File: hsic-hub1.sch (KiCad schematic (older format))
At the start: 32 parts

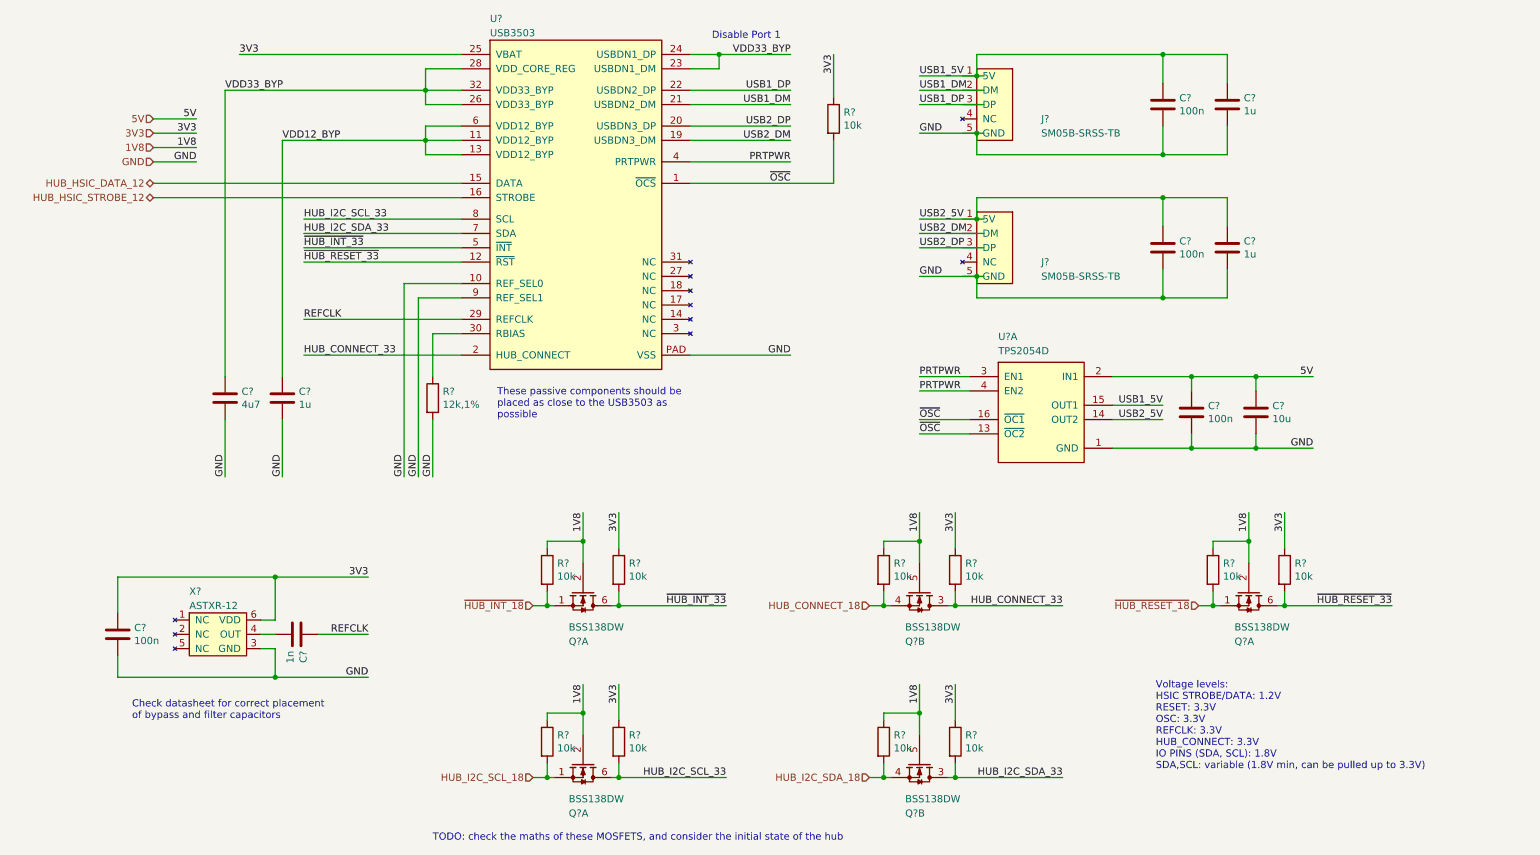
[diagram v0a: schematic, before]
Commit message: Add I2C level shifting and the two HSIC hubs.
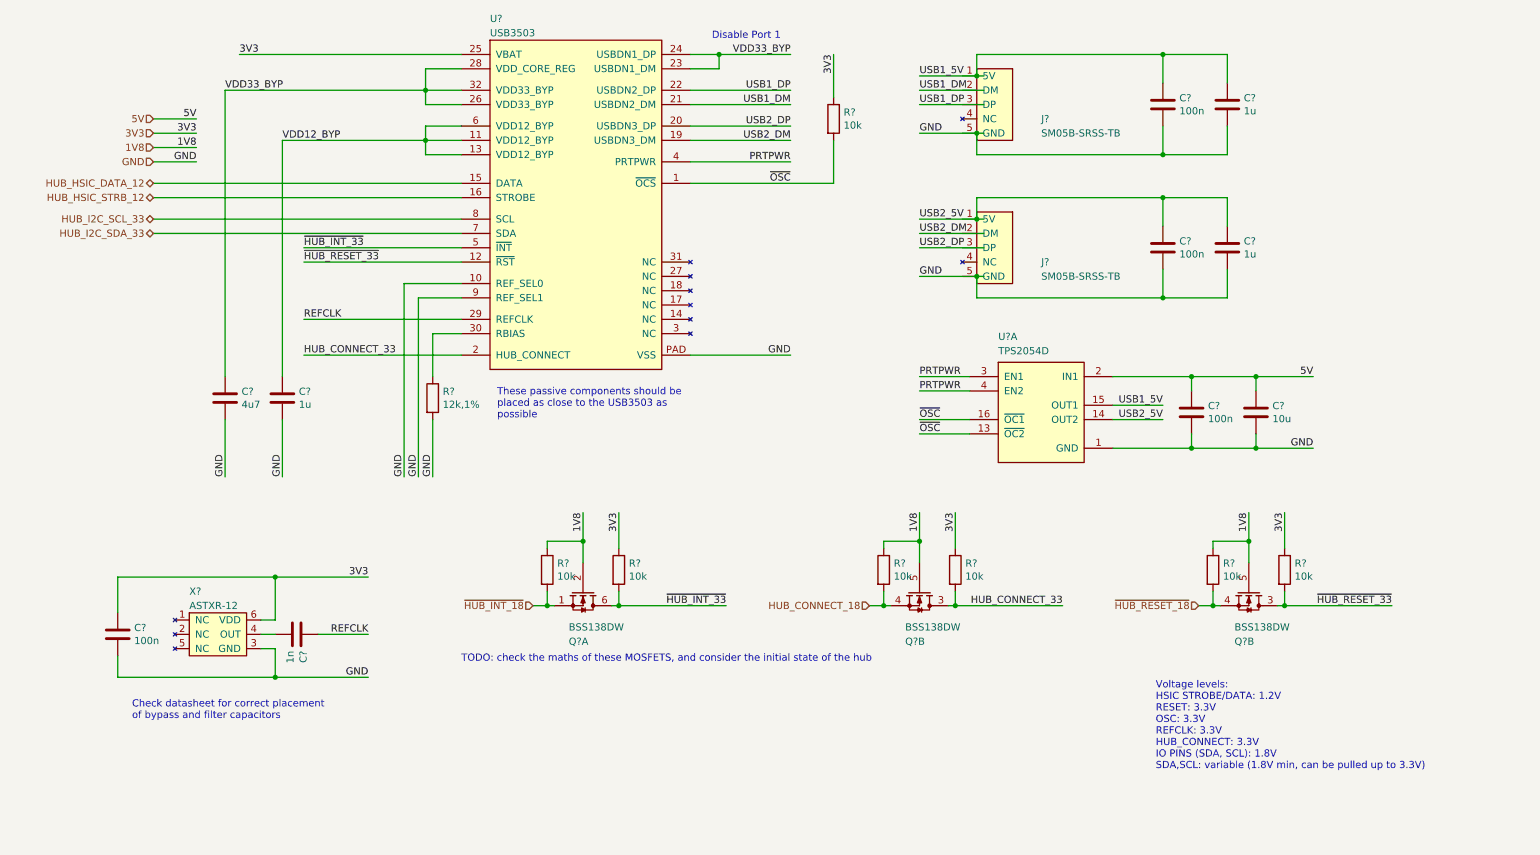
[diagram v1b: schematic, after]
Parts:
- removed Q? (x3): BSS138DW, symbol Drone:BSS138DW
- removed R? (x4): 10k, symbol Device:R
- added Q?: BSS138DW, symbol Drone:BSS138DW
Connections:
- net labels added: HUB_HSIC_STRB_12
- net labels removed: HUB_HSIC_STROBE_12, HUB_I2C_SCL_18, HUB_I2C_SDA_18
- wire segments 164 -> 142
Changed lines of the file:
@@
 $Descr A4 11693 8268
 encoding utf-8
-Sheet 2 3
+Sheet 4 4
 Title ""
 Date ""
@@
 	1400 1850 3550 1850
 Text HLabel 1400 1950 0    50   BiDi ~ 0
-HUB_HSIC_STROBE_12
+HUB_HSIC_STRB_12
 Text HLabel 1400 1850 0    50   BiDi ~ 0
 HUB_HSIC_DATA_12
@@
 AR Path="/5E2B9068/5E2F42C0" Ref="U?"  Part="1"
 AR Path="/5E2EDC4D/5E2F42C0" Ref="U?"  Part="1"
+AR Path="/5E349830/5E2F42C0" Ref="U?"  Part="1"
 F 0 "U?" H 3750 1000 50  0000 L CNN
 F 1 "USB3503" H 3750 900 50  0000 L CNN
@@
 	1700 1500 1400 1500
 Wire Wire Line
-	2450 2200 3550 2200
-Wire Wire Line
-	2450 2100 3550 2100
+	1400 2200 3550 2200
+Wire Wire Line
+	1400 2100 3550 2100
 Wire Wire Line
 	2450 2400 3550 2400
@@
 	1    0    0    -1
 $EndComp
-Text Label 2450 2100 0    50   ~ 0
-HUB_I2C_SCL_33
-Text Label 2450 2200 0    50   ~ 0
-HUB_I2C_SDA_33
 Text Label 2450 2300 0    50   ~ 0
 ~HUB_INT_33
@@
 HUB_CONNECT_33
 $Comp
-L Drone:BSS138DW Q?
-U 1 1 5E5F6987
-P 9050 4800
-F 0 "Q?" V 9300 4700 50  0000 L CNN
-F 1 "BSS138DW" V 9200 4700 50  0000 L CNN
-F 2 "" H 9150 4725 50  0001 L CIN
-F 3 "https://www.diodes.com/assets/Datasheets/ds30203.pdf" H 8950 4800 50  0001 L CNN
-	1    9050 4800
-	0    1    1    0
-$EndComp
-$Comp
 L Device:R R?
 U 1 1 5E5F698D
@@
 Text HLabel 8700 4800 0    50   Input ~ 0
 ~HUB_RESET_18
-$Comp
-L Drone:BSS138DW Q?
-U 2 1 5E636D9D
-P 6750 6000
-F 0 "Q?" V 7000 5900 50  0000 L CNN
-F 1 "BSS138DW" V 6900 5900 50  0000 L CNN
-F 2 "" H 6850 5925 50  0001 L CIN
-F 3 "https://www.diodes.com/assets/Datasheets/ds30203.pdf" H 6650 6000 50  0001 L CNN
-	2    6750 6000
-	0    1    1    0
-$EndComp
-$Comp
-L Device:R R?
-U 1 1 5E636DA3
-P 7000 5750
-F 0 "R?" H 7070 5796 50  0000 L CNN
-F 1 "10k" H 7070 5705 50  0000 L CNN
-F 2 "" V 6930 5750 50  0001 C CNN
-F 3 "~" H 7000 5750 50  0001 C CNN
-	1    7000 5750
-	1    0    0    -1
-$EndComp
-Text Label 7000 5350 3    50   ~ 0
-3V3
-Wire Wire Line
-	7000 5350 7000 5600
-Wire Wire Line
-	7000 5900 7000 6000
-Wire Wire Line
-	7000 6000 6950 6000
-Text Label 6750 5350 3    50   ~ 0
-1V8
-Wire Wire Line
-	6750 5350 6750 5550
-$Comp
-L Device:R R?
-U 1 1 5E636DAF
-P 6500 5750
-F 0 "R?" H 6570 5796 50  0000 L CNN
-F 1 "10k" H 6570 5705 50  0000 L CNN
-F 2 "" V 6430 5750 50  0001 C CNN
-F 3 "~" H 6500 5750 50  0001 C CNN
-	1    6500 5750
-	1    0    0    -1
-$EndComp
-Wire Wire Line
-	6500 5600 6500 5550
-Wire Wire Line
-	6500 5550 6750 5550
-Connection ~ 6750 5550
-Wire Wire Line
-	6750 5550 6750 5700
-Wire Wire Line
-	6550 6000 6500 6000
-Wire Wire Line
-	6500 6000 6500 5900
-Wire Wire Line
-	6500 6000 6400 6000
-Connection ~ 6500 6000
-Text HLabel 6400 6000 0    50   Input ~ 0
-HUB_I2C_SDA_18
-$Comp
-L Drone:BSS138DW Q?
-U 1 1 5E636DBE
-P 4400 6000
-F 0 "Q?" V 4650 5900 50  0000 L CNN
-F 1 "BSS138DW" V 4550 5900 50  0000 L CNN
-F 2 "" H 4500 5925 50  0001 L CIN
-F 3 "https://www.diodes.com/assets/Datasheets/ds30203.pdf" H 4300 6000 50  0001 L CNN
-	1    4400 6000
-	0    1    1    0
-$EndComp
-$Comp
-L Device:R R?
-U 1 1 5E636DC4
-P 4650 5750
-F 0 "R?" H 4720 5796 50  0000 L CNN
-F 1 "10k" H 4720 5705 50  0000 L CNN
-F 2 "" V 4580 5750 50  0001 C CNN
-F 3 "~" H 4650 5750 50  0001 C CNN
-	1    4650 5750
-	1    0    0    -1
-$EndComp
-Text Label 4650 5350 3    50   ~ 0
-3V3
-Wire Wire Line
-	4650 5350 4650 5600
-Wire Wire Line
-	4650 5900 4650 6000
-Wire Wire Line
-	4650 6000 4600 6000
-Text Label 4400 5350 3    50   ~ 0
-1V8
-Wire Wire Line
-	4400 5350 4400 5550
-$Comp
-L Device:R R?
-U 1 1 5E636DD0
-P 4150 5750
-F 0 "R?" H 4220 5796 50  0000 L CNN
-F 1 "10k" H 4220 5705 50  0000 L CNN
-F 2 "" V 4080 5750 50  0001 C CNN
-F 3 "~" H 4150 5750 50  0001 C CNN
-	1    4150 5750
-	1    0    0    -1
-$EndComp
-Wire Wire Line
-	4150 5600 4150 5550
-Wire Wire Line
-	4150 5550 4400 5550
-Connection ~ 4400 5550
-Wire Wire Line
-	4400 5550 4400 5700
-Wire Wire Line
-	4200 6000 4150 6000
-Wire Wire Line
-	4150 6000 4150 5900
-Wire Wire Line
-	4150 6000 4050 6000
-Connection ~ 4150 6000
-Wire Wire Line
-	4650 6000 5400 6000
-Connection ~ 4650 6000
-Text HLabel 4050 6000 0    50   Input ~ 0
-HUB_I2C_SCL_18
-Connection ~ 7000 6000
-Wire Wire Line
-	7000 6000 7750 6000
-Text Label 5400 6000 2    50   ~ 0
-HUB_I2C_SCL_33
-Text Label 7750 6000 2    50   ~ 0
-HUB_I2C_SDA_33
 Text Notes 8400 5950 0    50   ~ 0
 Voltage levels:\nHSIC STROBE/DATA: 1.2V\nRESET: 3.3V\nOSC: 3.3V\nREFCLK: 3.3V\nHUB_CONNECT: 3.3V\nIO PINS (SDA, SCL): 1.8V\nSDA,SCL: variable (1.8V min, can be pulled up to 3.3V)
-Text Notes 3350 6450 0    50   ~ 0
+Text Notes 3550 5200 0    50   ~ 0
 TODO: check the maths of these MOSFETS, and consider the initial state of the hub
+Text HLabel 1400 2100 0    50   BiDi ~ 0
+HUB_I2C_SCL_33
+Text HLabel 1400 2200 0    50   BiDi ~ 0
+HUB_I2C_SDA_33
+$Comp
+L Drone:BSS138DW Q?
+U 2 1 5E532DF9
+P 9050 4800
+AR Path="/5E2EDC4D/5E532DF9" Ref="Q?"  Part="2"
+AR Path="/5E349830/5E532DF9" Ref="Q?"  Part="2"
+F 0 "Q?" V 9300 4700 50  0000 L CNN
+F 1 "BSS138DW" V 9200 4700 50  0000 L CNN
+F 2 "" H 9150 4725 50  0001 L CIN
+F 3 "https://www.diodes.com/assets/Datasheets/ds30203.pdf" H 8950 4800 50  0001 L CNN
+	2    9050 4800
+	0    1    1    0
+$EndComp
 $EndSCHEMATC

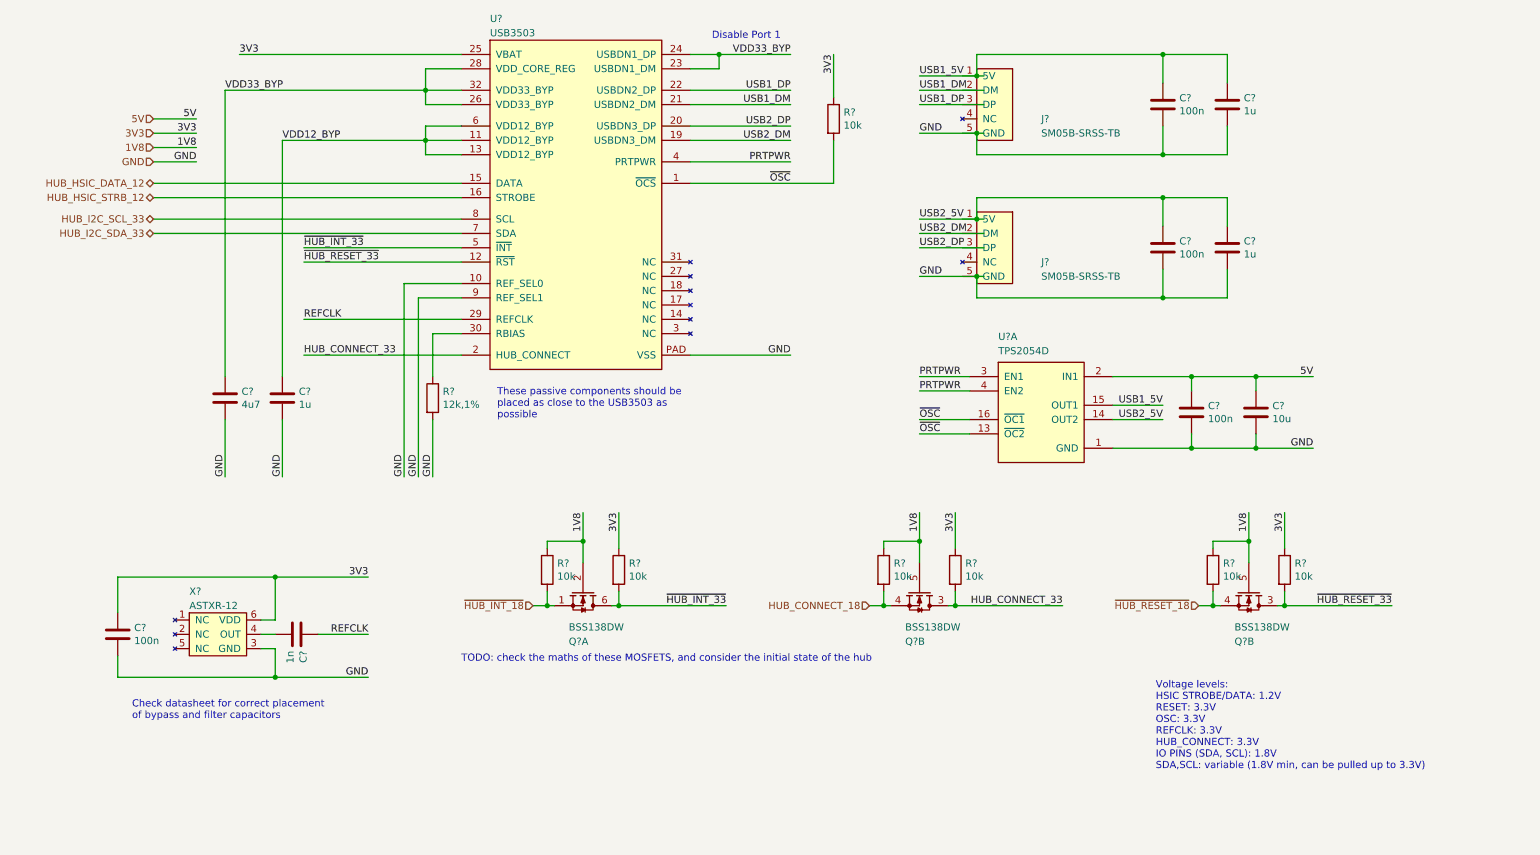
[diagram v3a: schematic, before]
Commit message: Added GPIO expander for hub signals.
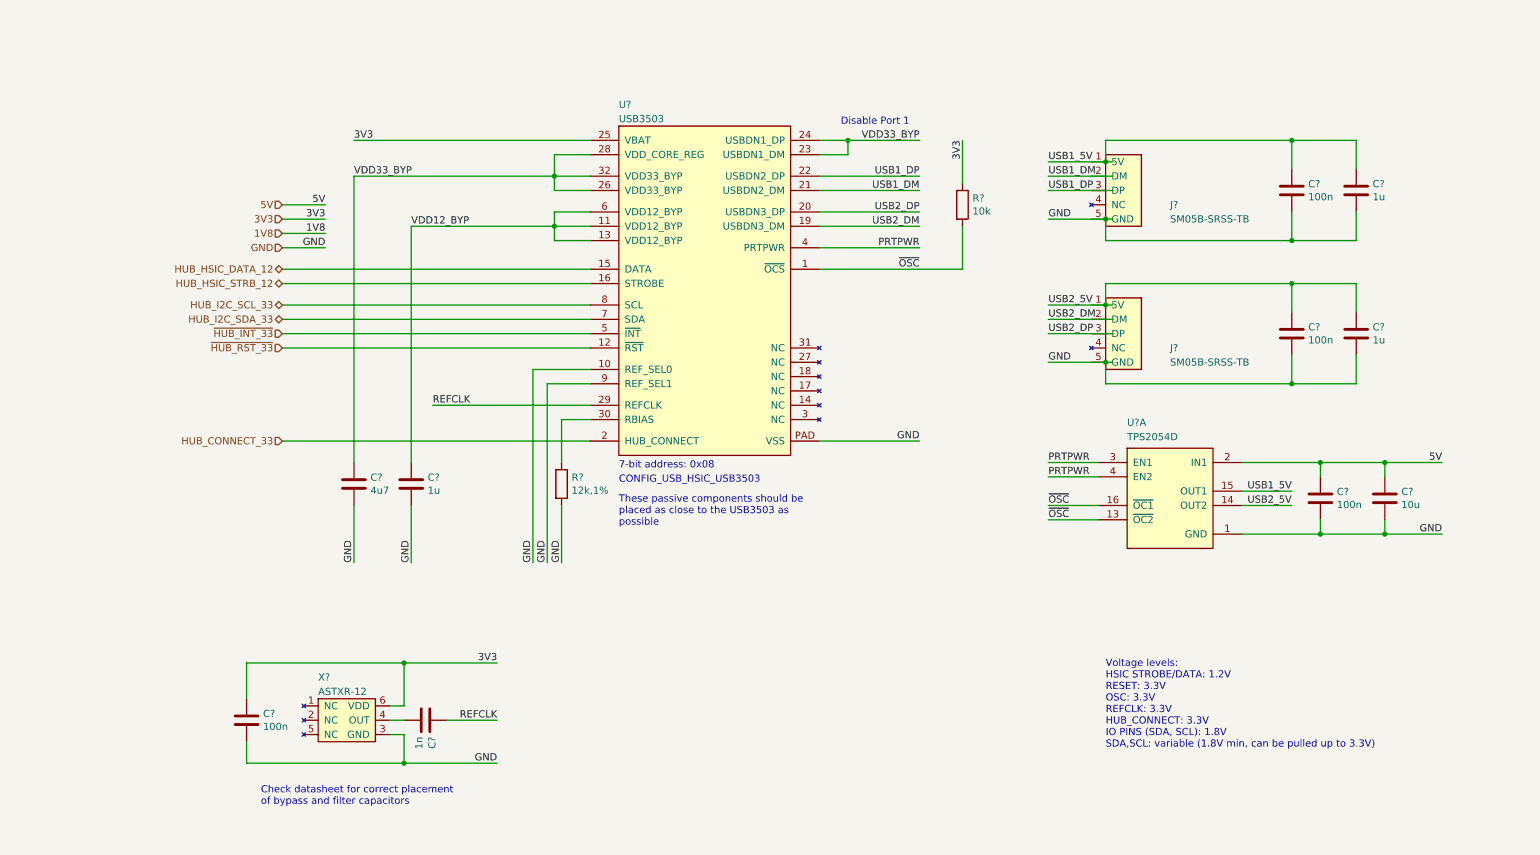
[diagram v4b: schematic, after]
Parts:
- removed Q? (x3): BSS138DW, symbol Drone:BSS138DW
- removed R? (x6): 10k, symbol Device:R
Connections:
- net labels added: ~HUB_RST_33
- net labels removed: HUB_CONNECT_18, ~HUB_INT_18, ~HUB_RESET_18, ~HUB_RESET_33
- wire segments 142 -> 109
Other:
- note added: "7-bit address: 0x08"
- note added: "CONFIG_USB_HSIC_USB3503"
- note removed: "TODO: check the maths of these MOSFETS, and consider the initial state of the hub"
- moved on the sheet: C?, J?, R?, U?, U?A, X?

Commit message: Use 0805 for all capacitors and resistors.
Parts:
- C? (x10): footprint (none) -> Capacitor_SMD:C_0805_2012Metric_Pad1.15x1.40mm_HandSolder; symbol Device:C -> Drone:CAP
- R? (x2): footprint (none) -> Resistor_SMD:R_0805_2012Metric_Pad1.15x1.40mm_HandSolder; symbol Device:R -> Drone:RES
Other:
- moved on the sheet: C?, J?, R?, U?, U?A, X?
